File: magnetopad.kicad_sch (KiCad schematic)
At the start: 17 parts, among them J1 Conn_01x04_Pin, J2 Conn_01x03_Socket, J3 Conn_01x03_Socket, SW1 SW_Push, SW2 SW_Push, SW3 SW_Push, SW4 SW_Push, U1 XIAO-RP2040-DIP

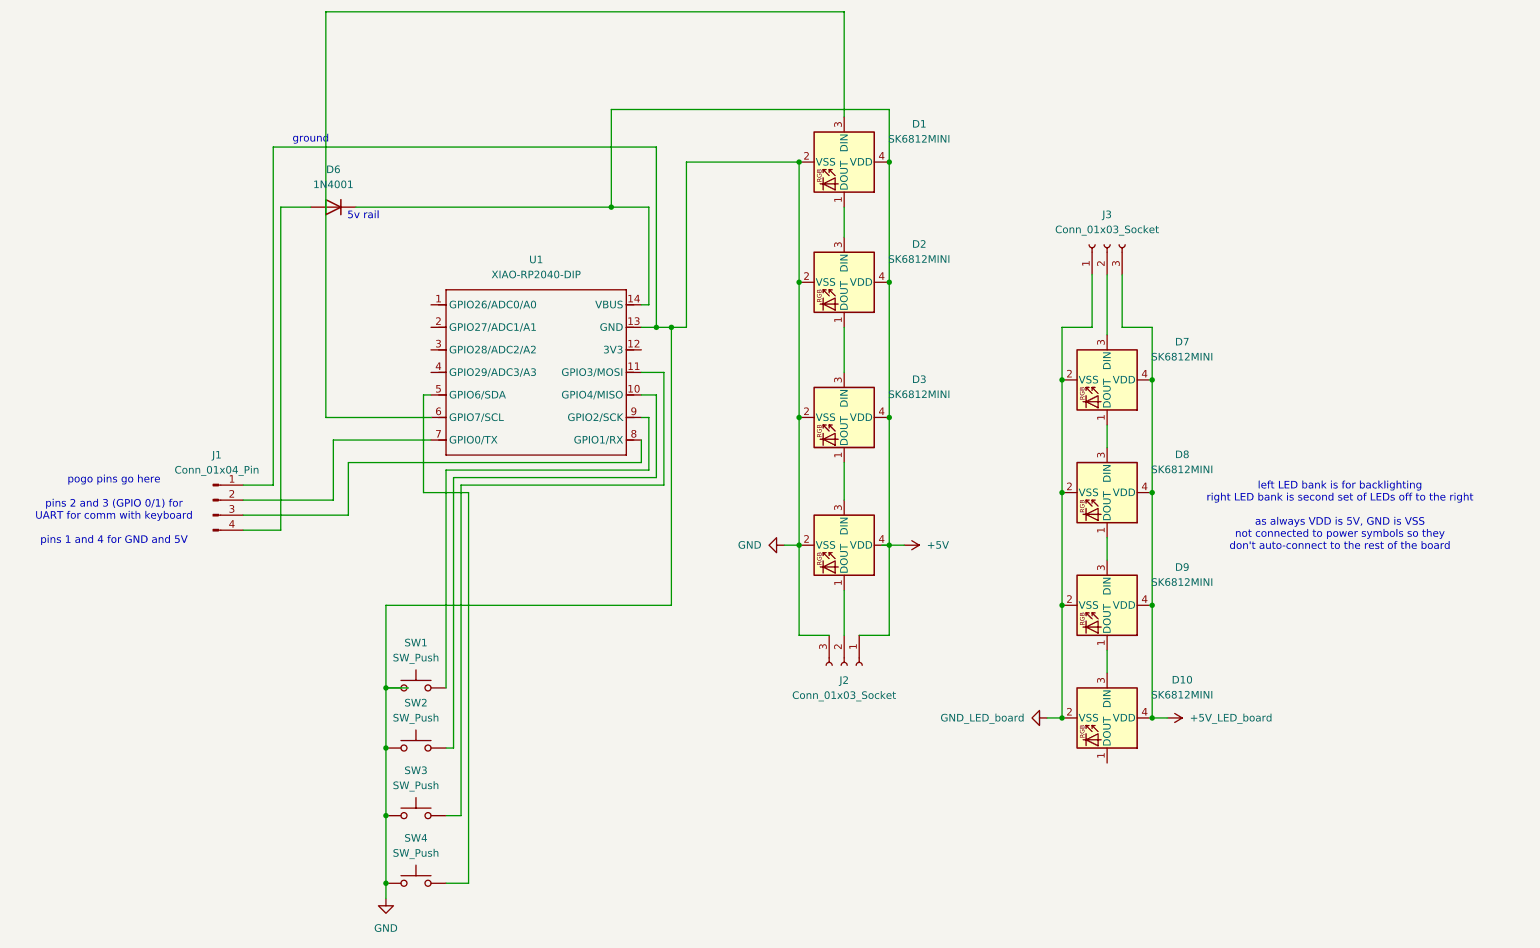
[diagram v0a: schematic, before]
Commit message: - update to use the right LEDs (SK6812MINI-E) (added marbastlib for that) - redo the board a bit so it actually lines up with the keycap grid decently - add art :3
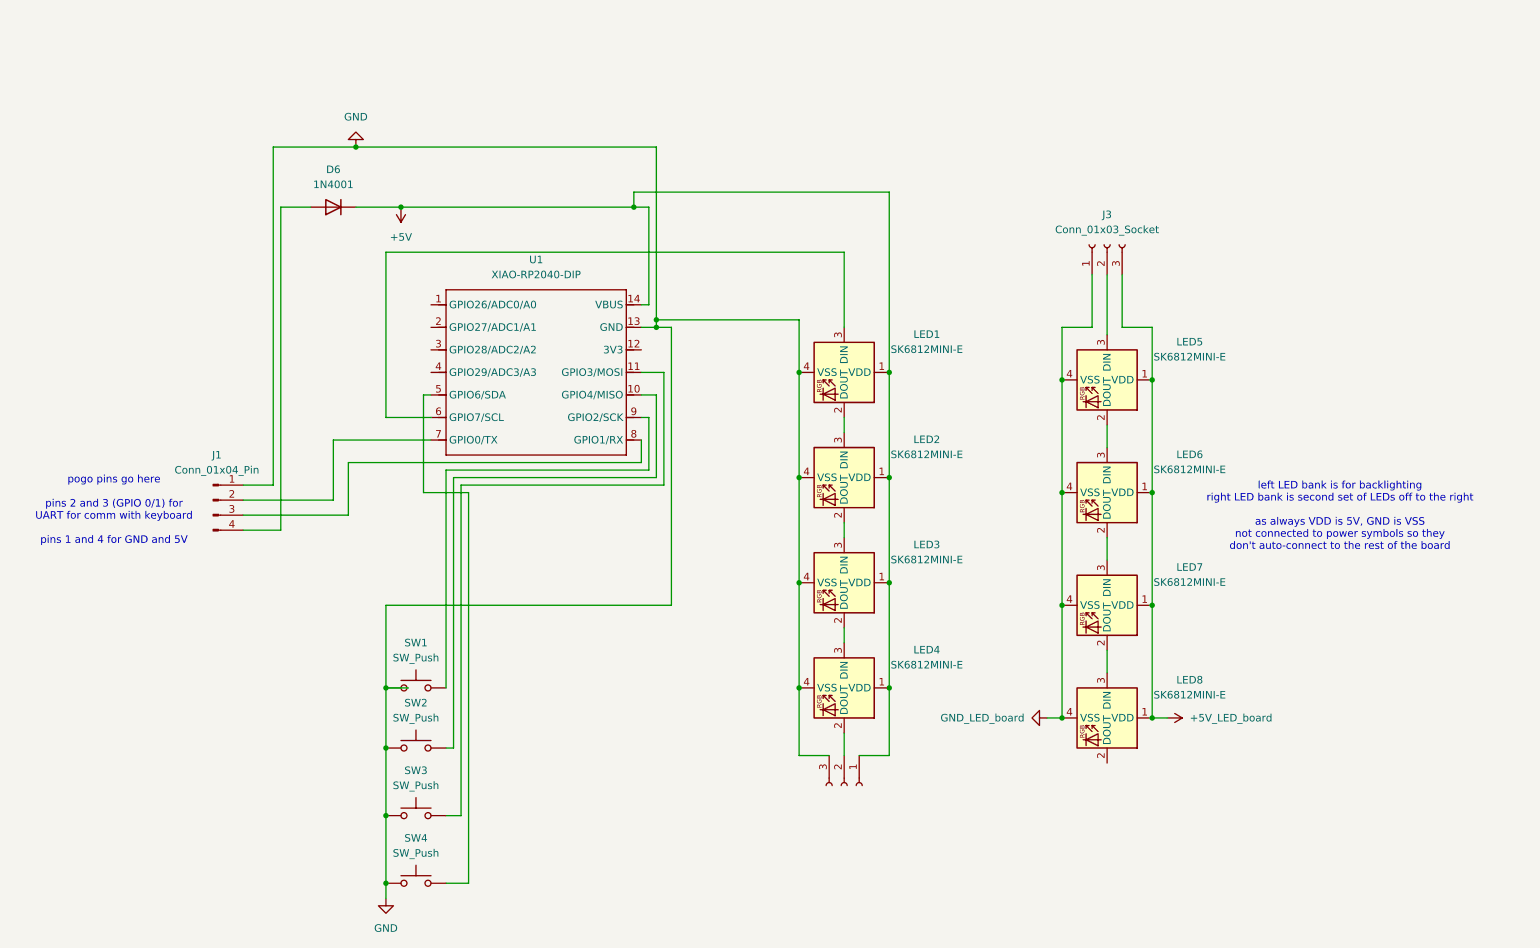
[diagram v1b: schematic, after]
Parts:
- removed D1, D10, D2, D3, D4, D7, D8, D9: SK6812MINI, LED_SMD:LED_SK6812MINI_PLCC4_3.5x3.5mm_P1.75mm, symbol LED:SK6812MINI
- added LED1, LED2, LED3, LED4, LED5, LED6, LED7, LED8: SK6812MINI-E, marbastlib-various:LED_6028R, symbol marbastlib-various:SK6812MINI-E
- J1: footprint Connector_PinHeader_2.54mm:PinHeader_1x04_P2.54mm_Vertical -> magnetopad:PinSocket_1x04_P1.8mm_Vertical
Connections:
- net +5V: now also LED1.1 (VDD), LED2.1 (VDD), LED3.1 (VDD), LED4.1 (VDD)
- net +5V_LED_board: now also LED5.1 (VDD), LED6.1 (VDD), LED7.1 (VDD), LED8.1 (VDD)
- net GND: now also LED1.4 (VSS), LED2.4 (VSS), LED3.4 (VSS), LED4.4 (VSS)
- net GND_LED_board: now also LED5.4 (VSS), LED6.4 (VSS), LED7.4 (VSS), LED8.4 (VSS)
- net at J3.2 (Pin_2): now also LED5.3 (DIN)
- net at J2.2 (Pin_2): now also LED4.2 (DOUT)
- net at U1.6 (GPIO7/SCL): now also LED1.3 (DIN)
- new net: LED2.2 (DOUT), LED3.3 (DIN)
- new net: LED1.2 (DOUT), LED2.3 (DIN)
- new net: LED3.2 (DOUT), LED4.3 (DIN)
- new net: LED7.2 (DOUT), LED8.3 (DIN)
- new net: LED6.2 (DOUT), LED7.3 (DIN)
- new net: LED5.2 (DOUT), LED6.3 (DIN)
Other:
- note removed: "5v rail"
- note removed: "ground"
